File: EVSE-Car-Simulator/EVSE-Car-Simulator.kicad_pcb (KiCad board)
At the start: 2 copper layers, 36.8 x 17.8 mm, 11 parts, among them J1 D-fault, J2 EV detect, J3 CP short, J4 EV ready, J5 Type 2, J6 CP-D, J7 PE-D

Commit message: CP Diag connector, closes #3
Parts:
- removed J7: PE-D, Pin_Headers:Pin_Header_Straight_1x01_Pitch2.54mm
- J6: value CP-D -> CP Diag; footprint Pin_Headers:Pin_Header_Straight_1x01_Pitch2.54mm -> Pin_Headers:Pin_Header_Straight_1x02_Pitch2.54mm
- moved J6 2.54 mm to (134.4, 96.5), turned to 90 degrees
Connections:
- J6 pad 1: CP -> PE
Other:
- board text added: "EVsim v0.3 Mathias Dalheimer"
- board text removed: "EVsim v0.2 Mathias Dalheimer"
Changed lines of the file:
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@@
     (thickness 1.6)
     (drawings 8)
-    (tracks 36)
+    (tracks 37)
     (zones 0)
-    (modules 11)
+    (modules 10)
     (nets 7)
   )
@@
       (drillshape 0)
       (scaleselection 1)
-      (outputdirectory ecs-gerber/v0.2/))
+      (outputdirectory ecs-gerber/v0.3/))
   )
   (net 0 "")
@@
     )
   )
-  (module Pin_Headers:Pin_Header_Straight_1x01_Pitch2.54mm (layer F.Cu)
-    (at 136.906 96.52 270)
-    (descr "Through hole straight pin header, 1x01, 2.54mm pitch, single row")
-    (tags "Through hole pin header THT 1x01 2.54mm single row")
-    (fp_text reference J6 (at 2.54 -1.27 270) (layer F.SilkS) hide
-      (effects (font (size 1 1) (thickness 0.15)))
-    )
-    (fp_text value CP-D (at 2.54 0 360) (layer F.SilkS)
-      (effects (font (size 1 1) (thickness 0.15)))
-    )
-    (fp_line (start -0.635 -1.27) (end 1.27 -1.27) (layer F.Fab) (width 0.1))
-    (fp_line (start 1.27 -1.27) (end 1.27 1.27) (layer F.Fab) (width 0.1))
-    (fp_line (start 1.27 1.27) (end -1.27 1.27) (layer F.Fab) (width 0.1))
-    (fp_line (start -1.27 1.27) (end -1.27 -0.635) (layer F.Fab) (width 0.1))
-    (fp_line (start -1.27 -0.635) (end -0.635 -1.27) (layer F.Fab) (width 0.1))
-    (fp_line (start -1.33 1.33) (end 1.33 1.33) (layer F.SilkS) (width 0.12))
-    (fp_line (start -1.33 1.27) (end -1.33 1.33) (layer F.SilkS) (width 0.12))
-    (fp_line (start 1.33 1.27) (end 1.33 1.33) (layer F.SilkS) (width 0.12))
-    (fp_line (start -1.33 1.27) (end 1.33 1.27) (layer F.SilkS) (width 0.12))
-    (fp_line (start -1.33 0) (end -1.33 -1.33) (layer F.SilkS) (width 0.12))
-    (fp_line (start -1.33 -1.33) (end 0 -1.33) (layer F.SilkS) (width 0.12))
-    (fp_line (start -1.8 -1.8) (end -1.8 1.8) (layer F.CrtYd) (width 0.05))
-    (fp_line (start -1.8 1.8) (end 1.8 1.8) (layer F.CrtYd) (width 0.05))
-    (fp_line (start 1.8 1.8) (end 1.8 -1.8) (layer F.CrtYd) (width 0.05))
-    (fp_line (start 1.8 -1.8) (end -1.8 -1.8) (layer F.CrtYd) (width 0.05))
-    (fp_text user %R (at 0 0 360) (layer F.Fab)
-      (effects (font (size 1 1) (thickness 0.15)))
-    )
-    (pad 1 thru_hole rect (at 0 0 270) (size 1.7 1.7) (drill 1) (layers *.Cu *.Mask)
-      (net 4 CP))
-    (model ${KISYS3DMOD}/Pin_Headers.3dshapes/Pin_Header_Straight_1x01_Pitch2.54mm.wrl
-      (at (xyz 0 0 0))
-      (scale (xyz 1 1 1))
-      (rotate (xyz 0 0 0))
-    )
-  )
-  (module Pin_Headers:Pin_Header_Straight_1x01_Pitch2.54mm (layer F.Cu)
-    (at 132.334 96.52 270)
-    (descr "Through hole straight pin header, 1x01, 2.54mm pitch, single row")
-    (tags "Through hole pin header THT 1x01 2.54mm single row")
-    (fp_text reference J7 (at 2.54 -1.27 270) (layer F.SilkS) hide
-      (effects (font (size 1 1) (thickness 0.15)))
-    )
-    (fp_text value PE-D (at 2.54 0 360) (layer F.SilkS)
-      (effects (font (size 1 1) (thickness 0.15)))
-    )
-    (fp_line (start -0.635 -1.27) (end 1.27 -1.27) (layer F.Fab) (width 0.1))
-    (fp_line (start 1.27 -1.27) (end 1.27 1.27) (layer F.Fab) (width 0.1))
-    (fp_line (start 1.27 1.27) (end -1.27 1.27) (layer F.Fab) (width 0.1))
-    (fp_line (start -1.27 1.27) (end -1.27 -0.635) (layer F.Fab) (width 0.1))
-    (fp_line (start -1.27 -0.635) (end -0.635 -1.27) (layer F.Fab) (width 0.1))
-    (fp_line (start -1.33 1.33) (end 1.33 1.33) (layer F.SilkS) (width 0.12))
-    (fp_line (start -1.33 1.27) (end -1.33 1.33) (layer F.SilkS) (width 0.12))
-    (fp_line (start 1.33 1.27) (end 1.33 1.33) (layer F.SilkS) (width 0.12))
-    (fp_line (start -1.33 1.27) (end 1.33 1.27) (layer F.SilkS) (width 0.12))
-    (fp_line (start -1.33 0) (end -1.33 -1.33) (layer F.SilkS) (width 0.12))
-    (fp_line (start -1.33 -1.33) (end 0 -1.33) (layer F.SilkS) (width 0.12))
-    (fp_line (start -1.8 -1.8) (end -1.8 1.8) (layer F.CrtYd) (width 0.05))
-    (fp_line (start -1.8 1.8) (end 1.8 1.8) (layer F.CrtYd) (width 0.05))
-    (fp_line (start 1.8 1.8) (end 1.8 -1.8) (layer F.CrtYd) (width 0.05))
-    (fp_line (start 1.8 -1.8) (end -1.8 -1.8) (layer F.CrtYd) (width 0.05))
-    (fp_text user %R (at 0 0 360) (layer F.Fab)
-      (effects (font (size 1 1) (thickness 0.15)))
-    )
-    (pad 1 thru_hole rect (at 0 0 270) (size 1.7 1.7) (drill 1) (layers *.Cu *.Mask)
-      (net 1 PE))
-    (model ${KISYS3DMOD}/Pin_Headers.3dshapes/Pin_Header_Straight_1x01_Pitch2.54mm.wrl
-      (at (xyz 0 0 0))
-      (scale (xyz 1 1 1))
-      (rotate (xyz 0 0 0))
-    )
-  )
   (module Resistors_THT:R_Axial_DIN0204_L3.6mm_D1.6mm_P7.62mm_Horizontal (layer F.Cu)
     (at 139.7 109.22 90)
@@
       (net 1 PE))
   )
-  (gr_text "EVsim v0.2\nMathias Dalheimer" (at 131.318 99.06 90) (layer B.Cu)
+  (module Pin_Headers:Pin_Header_Straight_1x02_Pitch2.54mm (layer F.Cu)
+    (at 134.366 96.52 90)
+    (descr "Through hole straight pin header, 1x02, 2.54mm pitch, single row")
+    (tags "Through hole pin header THT 1x02 2.54mm single row")
+    (fp_text reference J6 (at 0 -2.39 90) (layer F.Fab)
+      (effects (font (size 1 1) (thickness 0.15)))
+    )
+    (fp_text value "CP Diag" (at -2.54 1.27 180) (layer F.SilkS)
+      (effects (font (size 1 1) (thickness 0.15)))
+    )
+    (fp_line (start -1.27 -1.27) (end -1.27 3.81) (layer F.Fab) (width 0.1))
+    (fp_line (start -1.27 3.81) (end 1.27 3.81) (layer F.Fab) (width 0.1))
+    (fp_line (start 1.27 3.81) (end 1.27 -1.27) (layer F.Fab) (width 0.1))
+    (fp_line (start 1.27 -1.27) (end -1.27 -1.27) (layer F.Fab) (width 0.1))
+    (fp_line (start -1.39 1.27) (end -1.39 3.93) (layer F.SilkS) (width 0.12))
+    (fp_line (start -1.39 3.93) (end 1.39 3.93) (layer F.SilkS) (width 0.12))
+    (fp_line (start 1.39 3.93) (end 1.39 1.27) (layer F.SilkS) (width 0.12))
+    (fp_line (start 1.39 1.27) (end -1.39 1.27) (layer F.SilkS) (width 0.12))
+    (fp_line (start -1.39 0) (end -1.39 -1.39) (layer F.SilkS) (width 0.12))
+    (fp_line (start -1.39 -1.39) (end 0 -1.39) (layer F.SilkS) (width 0.12))
+    (fp_line (start -1.6 -1.6) (end -1.6 4.1) (layer F.CrtYd) (width 0.05))
+    (fp_line (start -1.6 4.1) (end 1.6 4.1) (layer F.CrtYd) (width 0.05))
+    (fp_line (start 1.6 4.1) (end 1.6 -1.6) (layer F.CrtYd) (width 0.05))
+    (fp_line (start 1.6 -1.6) (end -1.6 -1.6) (layer F.CrtYd) (width 0.05))
+    (pad 1 thru_hole rect (at 0 0 90) (size 1.7 1.7) (drill 1) (layers *.Cu *.Mask)
+      (net 1 PE))
+    (pad 2 thru_hole oval (at 0 2.54 90) (size 1.7 1.7) (drill 1) (layers *.Cu *.Mask)
+      (net 4 CP))
+    (model Pin_Headers.3dshapes/Pin_Header_Straight_1x02_Pitch2.54mm.wrl
+      (at (xyz 0 -0.05 0))
+      (scale (xyz 1 1 1))
+      (rotate (xyz 0 0 90))
+    )
+  )
+  (gr_text "EVsim v0.3\nMathias Dalheimer" (at 131.318 99.06 90) (layer B.Cu)
     (effects (font (size 0.8 0.8) (thickness 0.2)) (justify left mirror))
   )
@@
   (segment (start 139.192 99.06) (end 141.986 99.06) (width 0.5) (layer F.Cu) (net 4))
   (segment (start 127.508 102.87) (end 129.54 102.87) (width 0.5) (layer F.Cu) (net 4))
-  (segment (start 134.366 99.06) (end 136.906 96.52) (width 0.5) (layer F.Cu) (net 4))
-  (segment (start 133.35 99.06) (end 134.366 99.06) (width 0.5) (layer F.Cu) (net 4))
+  (segment (start 135.128 99.06) (end 136.906 97.282) (width 0.5) (layer F.Cu) (net 4))
+  (segment (start 133.35 99.06) (end 135.128 99.06) (width 0.5) (layer F.Cu) (net 4))
   (segment (start 129.54 102.87) (end 133.35 99.06) (width 0.5) (layer F.Cu) (net 4))
+  (segment (start 136.906 97.282) (end 136.906 96.52) (width 0.5) (layer F.Cu) (net 4))
   (segment (start 148.59 99.06) (end 148.59 96.52) (width 0.5) (layer B.Cu) (net 4))
   (segment (start 127.508 102.87) (end 128.016 102.87) (width 0.5) (layer F.Cu) (net 4))

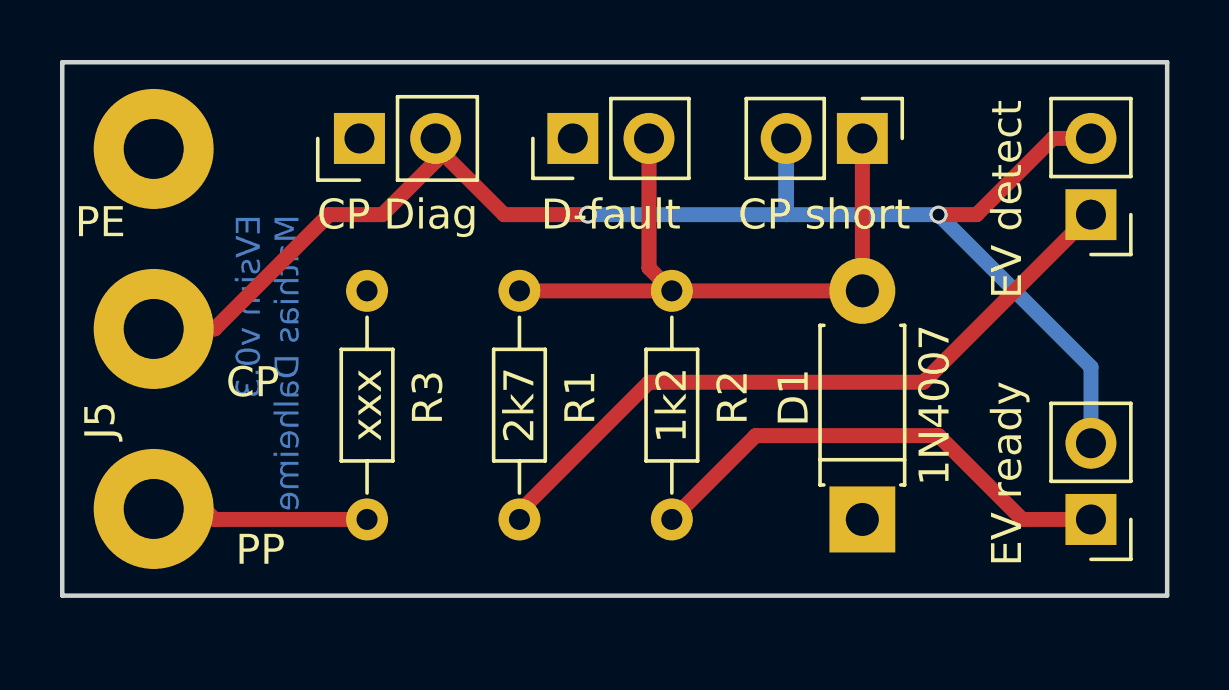
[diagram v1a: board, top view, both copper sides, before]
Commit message: updated schematic to reflect A/B/C/D/E states properly
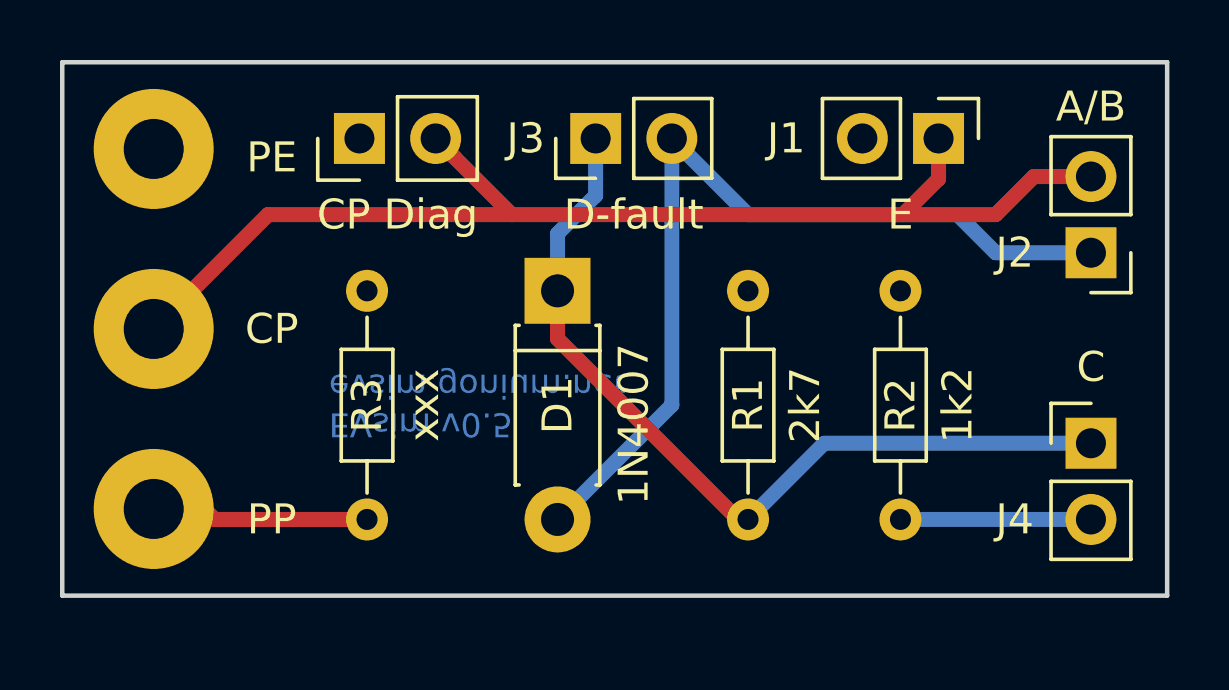
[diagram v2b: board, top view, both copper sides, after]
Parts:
- J1: value D-fault -> E
- J2: value EV detect -> A/B
- J3: value CP short -> D-fault
- J4: value EV ready -> C
- moved D1 12.7 mm to (141.0, 101.6), turned to 270 degrees
- moved J1 12.2 mm to (153.7, 96.5), turned to 270 degrees
- moved R1 10.8 mm to (147.3, 101.6), turned to 270 degrees
- moved R2 10.8 mm to (152.4, 101.6), turned to 270 degrees
- moved J3 8.89 mm to (142.2, 96.5), turned to 90 degrees
- moved J4 2.54 mm to (158.8, 106.7), turned to 0 degrees
- moved J2 1.27 mm to (158.8, 100.3)
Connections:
- D1 pad 1: PE -> Net-(D1-Pad1)
- D1 pad 2: N1 -> Net-(D1-Pad2)
- J1 pad 1: PE -> CP
- J1 pad 2: N1 -> PE
- J2 pad 1: Net-(J2-Pad1) -> Net-(D1-Pad2)
- J3 pad 1: N1 -> Net-(D1-Pad1)
- J3 pad 2: CP -> Net-(D1-Pad2)
- J4 pad 1: Net-(J4-Pad1) -> Net-(D1-Pad1)
- J4 pad 2: CP -> Net-(J4-Pad2)
- R1 pad 1: Net-(J2-Pad1) -> PE
- R1 pad 2: N1 -> Net-(D1-Pad1)
- R2 pad 1: Net-(J4-Pad1) -> PE
- R2 pad 2: N1 -> Net-(J4-Pad2)
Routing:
- net Net-(D1-Pad2): track 0.00 -> 29.8 mm
- net Net-(D1-Pad1): track 0.00 -> 28.5 mm
- net Net-(J2-Pad1): track 23.4 -> 0.00 mm
- net N1: track 21.9 -> 0.00 mm, vias 1 -> 0
- net Net-(J4-Pad1): track 16.3 -> 0.00 mm
- net CP: track 51.9 -> 40.5 mm, vias 2 -> 0
- net Net-(J4-Pad2): track 0.00 -> 6.35 mm
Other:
- board text added: "EVsim v0.5 evsim.gonium.net"
- board text removed: "EVsim v0.3 Mathias Dalheimer"
